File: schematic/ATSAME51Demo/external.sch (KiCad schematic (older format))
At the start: 29 parts, among them IC3 MCP2221-I_SL, J10 Conn_02x06_Odd_Even, J11 Conn_02x07_Odd_Even, J12 Conn_01x02, J13 Conn_01x08, J14 Conn_02x08_Odd_Even, J15 Conn_02x06_Odd_Even, J16 Conn_02x06_Odd_Even, J7 Conn_02x02_Odd_Even, J8 Conn_02x02_Odd_Even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

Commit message: Footprints assigned
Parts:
- C15: footprint (none) -> Capacitor_SMD:C_0603_1608Metric
- J10, J15, J16: footprint (none) -> Connector_PinHeader_2.54mm:PinHeader_2x06_P2.54mm_Vertical
- J11: footprint (none) -> Connector_PinHeader_2.54mm:PinHeader_2x07_P2.54mm_Vertical
- J12: footprint (none) -> Connector_PinHeader_2.54mm:PinHeader_1x02_P2.54mm_Vertical
- J14: footprint (none) -> Connector_PinHeader_2.54mm:PinHeader_2x08_P2.54mm_Vertical
- J7, J8: footprint (none) -> Connector_PinHeader_2.54mm:PinHeader_2x02_P2.54mm_Vertical
- R10, R12, R13, R15, R16, R17, R9: footprint (none) -> Resistor_SMD:R_0603_1608Metric
- R11, R14: value R -> 4k7; footprint (none) -> Resistor_SMD:R_0603_1608Metric
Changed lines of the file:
@@
 F 0 "C15" H 4065 1446 50  0000 L CNN
 F 1 "10uF" H 4065 1355 50  0000 L CNN
-F 2 "" H 3988 1250 50  0001 C CNN
+F 2 "Capacitor_SMD:C_0603_1608Metric" H 3988 1250 50  0001 C CNN
 F 3 "~" H 3950 1400 50  0001 C CNN
 	1    3950 1400
@@
 P 1650 6150
 F 0 "R11" H 1720 6196 50  0000 L CNN
-F 1 "R" H 1720 6105 50  0000 L CNN
-F 2 "" V 1580 6150 50  0001 C CNN
+F 1 "4k7" H 1720 6105 50  0000 L CNN
+F 2 "Resistor_SMD:R_0603_1608Metric" V 1580 6150 50  0001 C CNN
 F 3 "~" H 1650 6150 50  0001 C CNN
 	1    1650 6150
@@
 P 2250 6150
 F 0 "R14" H 2320 6196 50  0000 L CNN
-F 1 "R" H 2320 6105 50  0000 L CNN
-F 2 "" V 2180 6150 50  0001 C CNN
+F 1 "4k7" H 2320 6105 50  0000 L CNN
+F 2 "Resistor_SMD:R_0603_1608Metric" V 2180 6150 50  0001 C CNN
 F 3 "~" H 2250 6150 50  0001 C CNN
 	1    2250 6150
@@
 F 0 "J11" H 4150 5817 50  0000 C CNN
 F 1 "Conn_02x07_Odd_Even" H 4150 5726 50  0001 C CNN
-F 2 "" H 4100 5300 50  0001 C CNN
+F 2 "Connector_PinHeader_2.54mm:PinHeader_2x07_P2.54mm_Vertical" H 4100 5300 50  0001 C CNN
 F 3 "~" H 4100 5300 50  0001 C CNN
 	1    4100 5300
@@
 F 0 "J7" H 1950 5875 50  0000 C CNN
 F 1 "Conn_02x02_Odd_Even" H 1950 5876 50  0001 C CNN
-F 2 "" H 1900 5750 50  0001 C CNN
+F 2 "Connector_PinHeader_2.54mm:PinHeader_2x02_P2.54mm_Vertical" H 1900 5750 50  0001 C CNN
 F 3 "~" H 1900 5750 50  0001 C CNN
 	1    1900 5750
@@
 F 0 "J8" V 1950 6712 50  0000 R CNN
 F 1 "Conn_02x02_Odd_Even" H 1950 7026 50  0001 C CNN
-F 2 "" H 1900 6900 50  0001 C CNN
+F 2 "Connector_PinHeader_2.54mm:PinHeader_2x02_P2.54mm_Vertical" H 1900 6900 50  0001 C CNN
 F 3 "~" H 1900 6900 50  0001 C CNN
 	1    1900 6900
@@
 F 0 "R9" H 1100 3400 50  0000 L CNN
 F 1 "100k" H 1000 3300 50  0000 L CNN
-F 2 "" V 1180 3350 50  0001 C CNN
+F 2 "Resistor_SMD:R_0603_1608Metric" V 1180 3350 50  0001 C CNN
 F 3 "~" H 1250 3350 50  0001 C CNN
 	1    1250 3350
@@
 F 0 "R16" H 4220 3396 50  0000 L CNN
 F 1 "10k" H 4220 3305 50  0000 L CNN
-F 2 "" V 4080 3350 50  0001 C CNN
+F 2 "Resistor_SMD:R_0603_1608Metric" V 4080 3350 50  0001 C CNN
 F 3 "~" H 4150 3350 50  0001 C CNN
 	1    4150 3350
@@
 F 0 "R10" H 1350 3500 50  0000 L CNN
 F 1 "100k" V 1400 3250 50  0000 L CNN
-F 2 "" V 1430 3350 50  0001 C CNN
+F 2 "Resistor_SMD:R_0603_1608Metric" V 1430 3350 50  0001 C CNN
 F 3 "~" H 1500 3350 50  0001 C CNN
 	1    1500 3350
@@
 F 0 "R12" H 1600 3500 50  0000 L CNN
 F 1 "100k" V 1650 3250 50  0000 L CNN
-F 2 "" V 1680 3350 50  0001 C CNN
+F 2 "Resistor_SMD:R_0603_1608Metric" V 1680 3350 50  0001 C CNN
 F 3 "~" H 1750 3350 50  0001 C CNN
 	1    1750 3350
@@
 F 0 "R13" H 2070 3396 50  0000 L CNN
 F 1 "10k" H 2050 3300 50  0000 L CNN
-F 2 "" V 1930 3350 50  0001 C CNN
+F 2 "Resistor_SMD:R_0603_1608Metric" V 1930 3350 50  0001 C CNN
 F 3 "~" H 2000 3350 50  0001 C CNN
 	1    2000 3350
@@
 F 0 "R15" H 3700 3400 50  0000 L CNN
 F 1 "100k" H 3600 3300 50  0000 L CNN
-F 2 "" V 3780 3350 50  0001 C CNN
+F 2 "Resistor_SMD:R_0603_1608Metric" V 3780 3350 50  0001 C CNN
 F 3 "~" H 3850 3350 50  0001 C CNN
 	1    3850 3350
@@
 F 0 "J10" V 2850 3812 50  0000 R CNN
 F 1 "Conn_02x06_Odd_Even" V 2805 3812 50  0001 R CNN
-F 2 "" H 2800 4200 50  0001 C CNN
+F 2 "Connector_PinHeader_2.54mm:PinHeader_2x06_P2.54mm_Vertical" H 2800 4200 50  0001 C CNN
 F 3 "~" H 2800 4200 50  0001 C CNN
 	1    2800 4200
@@
 F 0 "J14" H 5750 5725 50  0000 C CNN
 F 1 "Conn_02x08_Odd_Even" H 5750 5726 50  0001 C CNN
-F 2 "" H 5700 5300 50  0001 C CNN
+F 2 "Connector_PinHeader_2.54mm:PinHeader_2x08_P2.54mm_Vertical" H 5700 5300 50  0001 C CNN
 F 3 "~" H 5700 5300 50  0001 C CNN
 	1    5700 5300
@@
 F 0 "J15" H 7600 5525 50  0000 C CNN
 F 1 "Conn_02x06_Odd_Even" H 7600 5526 50  0001 C CNN
-F 2 "" H 7550 5200 50  0001 C CNN
+F 2 "Connector_PinHeader_2.54mm:PinHeader_2x06_P2.54mm_Vertical" H 7550 5200 50  0001 C CNN
 F 3 "~" H 7550 5200 50  0001 C CNN
 	1    7550 5200
@@
 F 0 "J16" H 9400 5525 50  0000 C CNN
 F 1 "Conn_02x06_Odd_Even" H 9400 5526 50  0001 C CNN
-F 2 "" H 9350 5200 50  0001 C CNN
+F 2 "Connector_PinHeader_2.54mm:PinHeader_2x06_P2.54mm_Vertical" H 9350 5200 50  0001 C CNN
 F 3 "~" H 9350 5200 50  0001 C CNN
 	1    9350 5200
@@
 F 0 "R17" H 4670 6596 50  0000 L CNN
 F 1 "10k" H 4670 6505 50  0000 L CNN
-F 2 "" V 4530 6550 50  0001 C CNN
+F 2 "Resistor_SMD:R_0603_1608Metric" V 4530 6550 50  0001 C CNN
 F 3 "~" H 4600 6550 50  0001 C CNN
 	1    4600 6550
@@
 F 0 "J12" V 4518 5912 50  0000 R CNN
 F 1 "Conn_01x02" V 4473 5912 50  0001 R CNN
-F 2 "" H 4600 6100 50  0001 C CNN
+F 2 "Connector_PinHeader_2.54mm:PinHeader_1x02_P2.54mm_Vertical" H 4600 6100 50  0001 C CNN
 F 3 "~" H 4600 6100 50  0001 C CNN
 	1    4600 6100

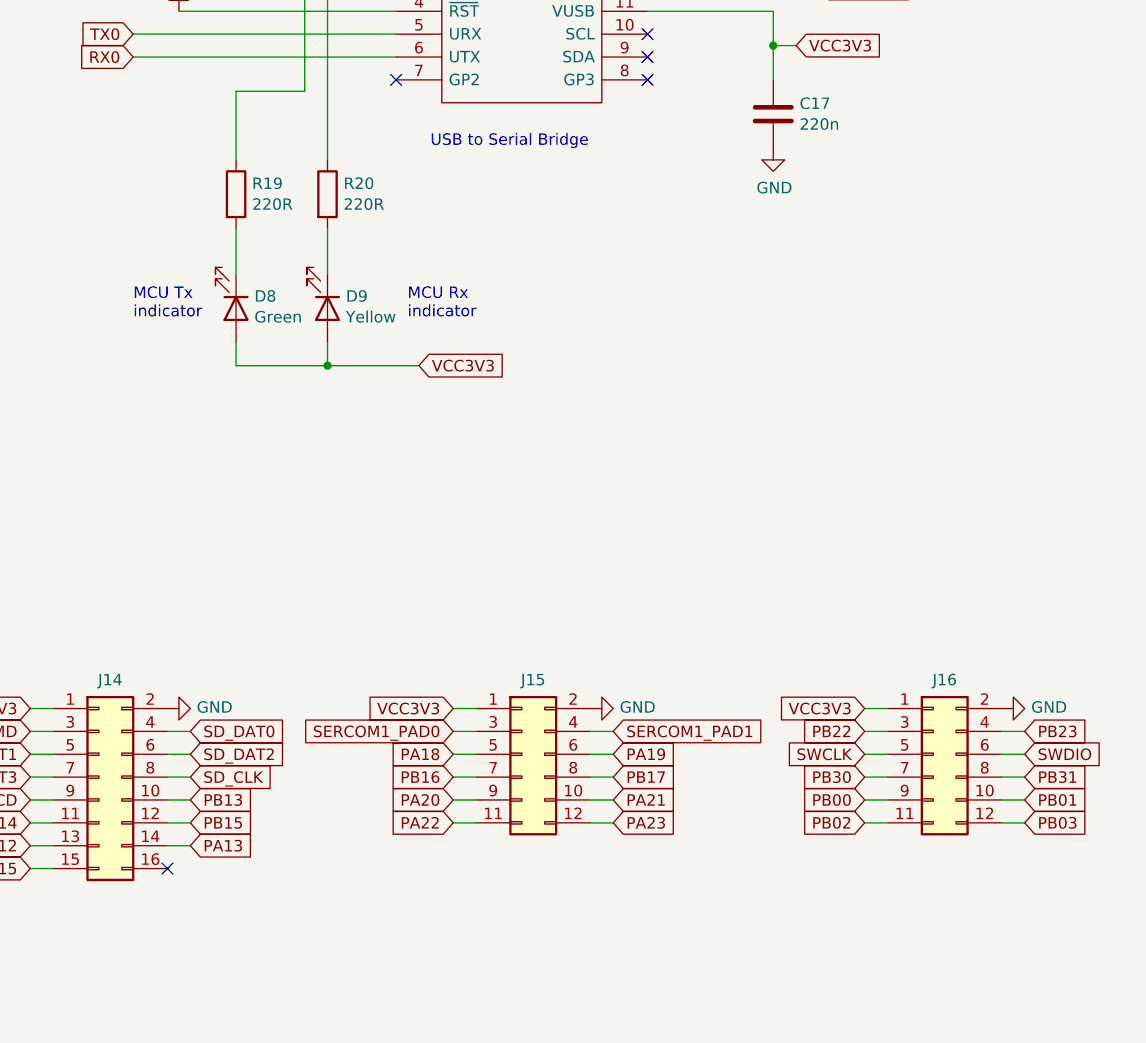
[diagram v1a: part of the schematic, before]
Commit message: Removed USB detect
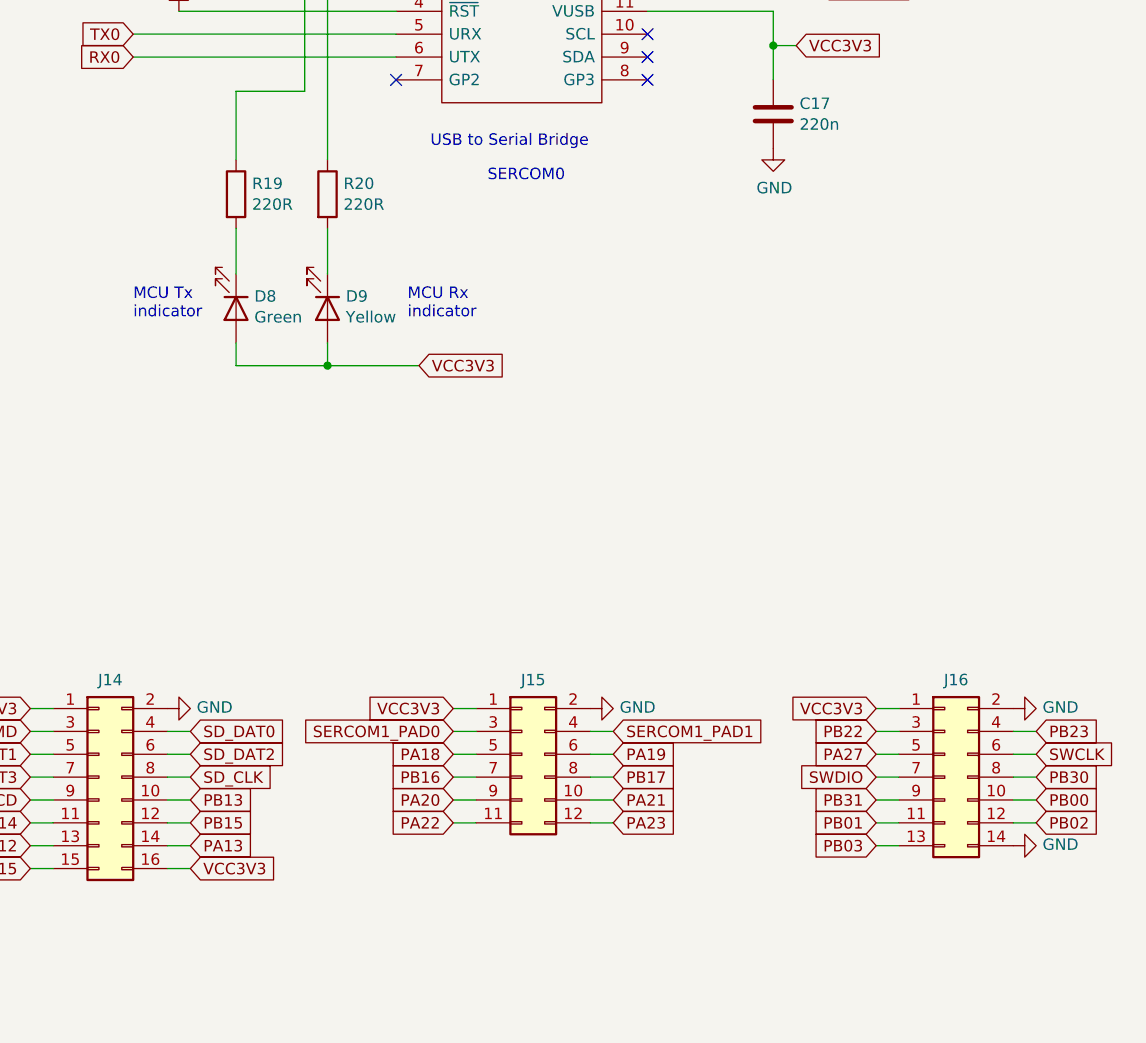
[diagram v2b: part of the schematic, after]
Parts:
- removed J16: Conn_02x06_Odd_Even, Connector_PinHeader_2.54mm:PinHeader_2x06_P2.54mm_Vertical, symbol Connector_Generic:Conn_02x06_Odd_Even
- added J16: Conn_02x07_Odd_Even, symbol Connector_Generic:Conn_02x07_Odd_Even
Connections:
- net GND: now also J16.14 (Pin_14), J16.2 (Pin_2)
- net PB00: now also J16.10 (Pin_10)
- net PB01: now also J16.11 (Pin_11)
- net PB02: now also J16.12 (Pin_12)
- net PB03: now also J16.13 (Pin_13)
- net PB22: now also J16.3 (Pin_3)
- net PB23: now also J16.4 (Pin_4)
- net PB30: now also J16.8 (Pin_8)
- net PB31: now also J16.9 (Pin_9)
- net SWCLK: now also J16.6 (Pin_6)
- net SWDIO: now also J16.7 (Pin_7)
- net VCC3V3: now also J14.16 (Pin_16), J16.1 (Pin_1)
- new net PA27: J16.5 (Pin_5)
- no-connect marks 8 -> 7
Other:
- note added: "SERCOM0"
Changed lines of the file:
@@
 encoding utf-8
 Sheet 3 3
-Title "SAMduino"
-Date "2021-10-22"
+Title "ATSAME51 Demo Board"
+Date "2021-10-25"
 Rev "1.0"
 Comp "Quantum Embedded Systems"
@@
 	1    0    0    -1
 $EndComp
-$Comp
-L Connector_Generic:Conn_02x06_Odd_Even J16
-U 1 1 6179D1B9
-P 9350 5200
-F 0 "J16" H 9400 5525 50  0000 C CNN
-F 1 "Conn_02x06_Odd_Even" H 9400 5526 50  0001 C CNN
-F 2 "Connector_PinHeader_2.54mm:PinHeader_2x06_P2.54mm_Vertical" H 9350 5200 50  0001 C CNN
-F 3 "~" H 9350 5200 50  0001 C CNN
-	1    9350 5200
-	1    0    0    -1
-$EndComp
 Text GLabel 5400 5000 0    50   Input ~ 0
 VCC3V3
 Text GLabel 7250 5000 0    50   Input ~ 0
 VCC3V3
-Text GLabel 9050 5000 0    50   Input ~ 0
+Text GLabel 9100 5000 0    50   Input ~ 0
 VCC3V3
 $Comp
@@
 L power:GND #PWR040
 U 1 1 617B4203
-P 9650 5000
-F 0 "#PWR040" H 9650 4750 50  0001 C CNN
-F 1 "GND" V 9655 4872 50  0000 R CNN
-F 2 "" H 9650 5000 50  0001 C CNN
-F 3 "" H 9650 5000 50  0001 C CNN
-	1    9650 5000
+P 9700 5000
+F 0 "#PWR040" H 9700 4750 50  0001 C CNN
+F 1 "GND" V 9705 4872 50  0000 R CNN
+F 2 "" H 9700 5000 50  0001 C CNN
+F 3 "" H 9700 5000 50  0001 C CNN
+	1    9700 5000
 	0    -1   -1   0
 $EndComp
@@
 Wire Wire Line
 	7850 5100 7950 5100
-Text GLabel 9050 5100 0    50   Input ~ 0
+Text GLabel 9100 5100 0    50   Input ~ 0
 PB22
-Text GLabel 9750 5100 2    50   Input ~ 0
+Text GLabel 9800 5100 2    50   Input ~ 0
 PB23
-Text GLabel 9050 5200 0    50   Input ~ 0
+Text GLabel 9800 5200 2    50   Input ~ 0
 SWCLK
-Text GLabel 9750 5200 2    50   Input ~ 0
+Text GLabel 9100 5300 0    50   Input ~ 0
 SWDIO
-Text GLabel 9050 5300 0    50   Input ~ 0
+Text GLabel 9800 5300 2    50   Input ~ 0
 PB30
-Text GLabel 9750 5300 2    50   Input ~ 0
+Text GLabel 9100 5400 0    50   Input ~ 0
 PB31
-Text GLabel 9050 5400 0    50   Input ~ 0
+Text GLabel 9800 5400 2    50   Input ~ 0
 PB00
-Text GLabel 9750 5400 2    50   Input ~ 0
+Text GLabel 9100 5500 0    50   Input ~ 0
 PB01
-Text GLabel 9050 5500 0    50   Input ~ 0
+Text GLabel 9800 5500 2    50   Input ~ 0
 PB02
-Text GLabel 9750 5500 2    50   Input ~ 0
+Text GLabel 9100 5600 0    50   Input ~ 0
 PB03
 Wire Wire Line
-	9150 5000 9050 5000
-Wire Wire Line
-	9050 5100 9150 5100
-Wire Wire Line
-	9150 5200 9050 5200
-Wire Wire Line
-	9050 5300 9150 5300
-Wire Wire Line
-	9150 5400 9050 5400
-Wire Wire Line
-	9050 5500 9150 5500
-Wire Wire Line
-	9650 5500 9750 5500
-Wire Wire Line
-	9750 5400 9650 5400
-Wire Wire Line
-	9650 5300 9750 5300
-Wire Wire Line
-	9750 5200 9650 5200
-Wire Wire Line
-	9650 5100 9750 5100
+	9200 5000 9100 5000
+Wire Wire Line
+	9100 5100 9200 5100
+Wire Wire Line
+	9700 5200 9800 5200
+Wire Wire Line
+	9800 5300 9700 5300
+Wire Wire Line
+	9700 5400 9800 5400
+Wire Wire Line
+	9800 5500 9700 5500
+Wire Wire Line
+	9200 5600 9100 5600
+Wire Wire Line
+	9100 5500 9200 5500
+Wire Wire Line
+	9200 5400 9100 5400
+Wire Wire Line
+	9100 5300 9200 5300
+Wire Wire Line
+	9700 5100 9800 5100
 $Comp
 L Connector_Generic:Conn_01x08 J13
@@
 NoConn ~ 4900 7100
 NoConn ~ 4900 7300
-NoConn ~ 6000 5700
 Text Notes 4500 7800 0    50   ~ 0
 Program/Debug
+$Comp
+L Connector_Generic:Conn_02x07_Odd_Even J16
+U 1 1 61786159
+P 9400 5300
+F 0 "J16" H 9450 5725 50  0000 C CNN
+F 1 "Conn_02x07_Odd_Even" H 9450 5726 50  0001 C CNN
+F 2 "" H 9400 5300 50  0001 C CNN
+F 3 "~" H 9400 5300 50  0001 C CNN
+	1    9400 5300
+	1    0    0    -1
+$EndComp
+Text GLabel 9100 5200 0    50   Input ~ 0
+PA27
+$Comp
+L power:GND #PWR0101
+U 1 1 617DA1A7
+P 9700 5600
+F 0 "#PWR0101" H 9700 5350 50  0001 C CNN
+F 1 "GND" V 9705 5472 50  0000 R CNN
+F 2 "" H 9700 5600 50  0001 C CNN
+F 3 "" H 9700 5600 50  0001 C CNN
+	1    9700 5600
+	0    -1   -1   0
+$EndComp
+Text GLabel 6100 5700 2    50   Input ~ 0
+VCC3V3
+Wire Wire Line
+	6000 5700 6100 5700
+Wire Wire Line
+	9100 5200 9200 5200
+Text Notes 7400 2700 0    50   ~ 0
+SERCOM0
 $EndSCHEMATC

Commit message: First draft PCB layout
Still needs silkscreen cleanup
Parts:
- J16: footprint (none) -> Connector_PinHeader_2.54mm:PinHeader_2x07_P2.54mm_Vertical
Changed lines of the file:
@@
 F 0 "J16" H 9450 5725 50  0000 C CNN
 F 1 "Conn_02x07_Odd_Even" H 9450 5726 50  0001 C CNN
-F 2 "" H 9400 5300 50  0001 C CNN
+F 2 "Connector_PinHeader_2.54mm:PinHeader_2x07_P2.54mm_Vertical" H 9400 5300 50  0001 C CNN
 F 3 "~" H 9400 5300 50  0001 C CNN
 	1    9400 5300

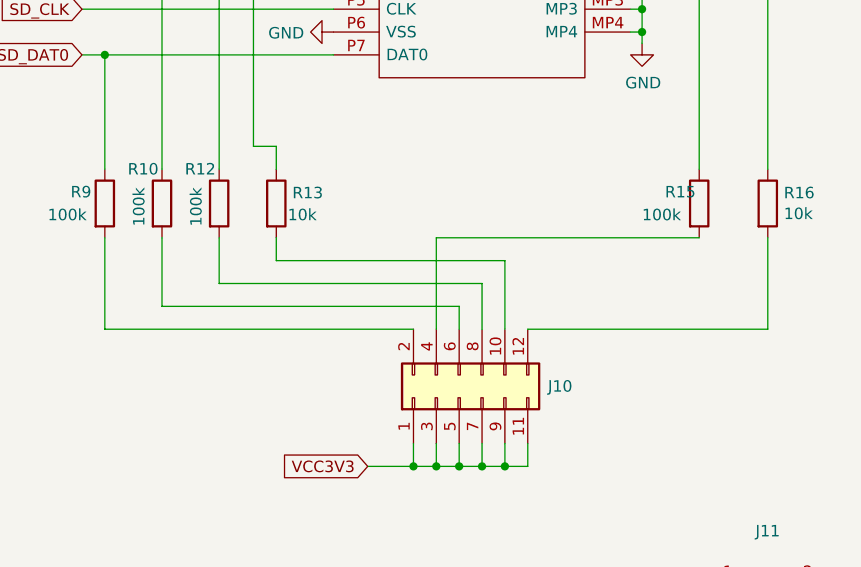
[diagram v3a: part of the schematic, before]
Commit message: Moved SD card back from edge
Rearranged some connections to improve routing
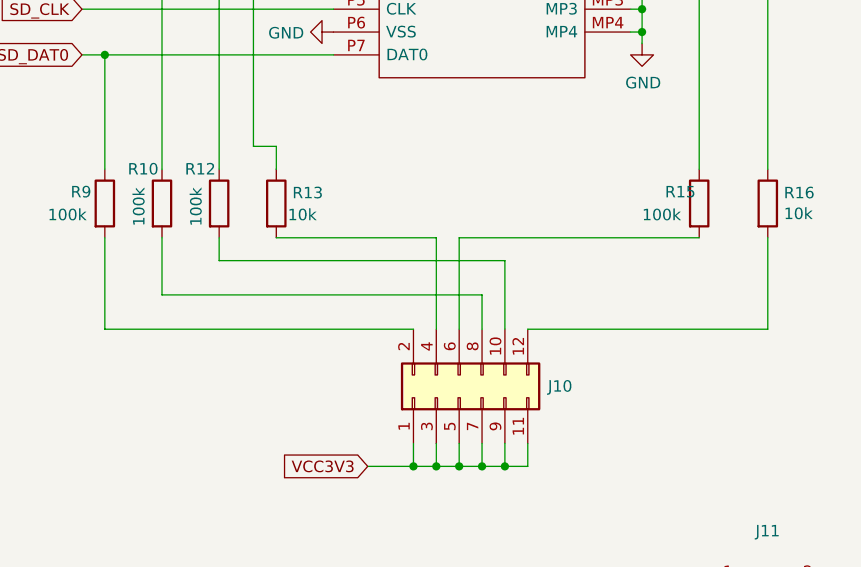
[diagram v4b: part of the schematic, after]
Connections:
- net at R10.2: now also J10.8 (Pin_8); no longer J10.6 (Pin_6)
- net at R12.2: now also J10.10 (Pin_10); no longer J10.8 (Pin_8)
- net at R13.2: now also J10.4 (Pin_4); no longer J10.10 (Pin_10)
- net at R15.2: now also J10.6 (Pin_6); no longer J10.4 (Pin_4)
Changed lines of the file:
@@
 	1250 2700 2250 2700
-Wire Wire Line
-	1250 3500 1250 3900
-Wire Wire Line
-	1250 3900 2600 3900
-Wire Wire Line
-	1500 3500 1500 3800
-Wire Wire Line
-	1500 3800 2800 3800
-Wire Wire Line
-	2800 3800 2800 3900
-Wire Wire Line
-	1750 3500 1750 3700
-Wire Wire Line
-	1750 3700 2900 3700
-Wire Wire Line
-	2900 3700 2900 3900
-Wire Wire Line
-	2000 3500 2000 3600
-Wire Wire Line
-	2000 3600 3000 3600
-Wire Wire Line
-	3000 3600 3000 3900
 Wire Wire Line
 	1500 3200 1500 2100
@@
 Wire Wire Line
 	4150 2200 4350 2200
-Wire Wire Line
-	3850 3500 2700 3500
-Wire Wire Line
-	2700 3500 2700 3900
 Wire Wire Line
 	3100 3900 4150 3900
@@
 Text Notes 7400 2700 0    50   ~ 0
 SERCOM0
+Wire Wire Line
+	1250 3900 2600 3900
+Wire Wire Line
+	1250 3500 1250 3900
+Wire Wire Line
+	2000 3500 2700 3500
+Wire Wire Line
+	2700 3500 2700 3900
+Wire Wire Line
+	3850 3500 2800 3500
+Wire Wire Line
+	2800 3500 2800 3900
+Wire Wire Line
+	1500 3500 1500 3750
+Wire Wire Line
+	1500 3750 2900 3750
+Wire Wire Line
+	2900 3750 2900 3900
+Wire Wire Line
+	1750 3500 1750 3600
+Wire Wire Line
+	1750 3600 3000 3600
+Wire Wire Line
+	3000 3600 3000 3900
 $EndSCHEMATC
